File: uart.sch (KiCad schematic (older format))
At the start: 17 parts, among them P1 USB_OTG, U2 FOD817, U3 FOD817, U4 FOD817, U5 FOD817, U6 MCP2200, X1 CRYSTAL_SMD

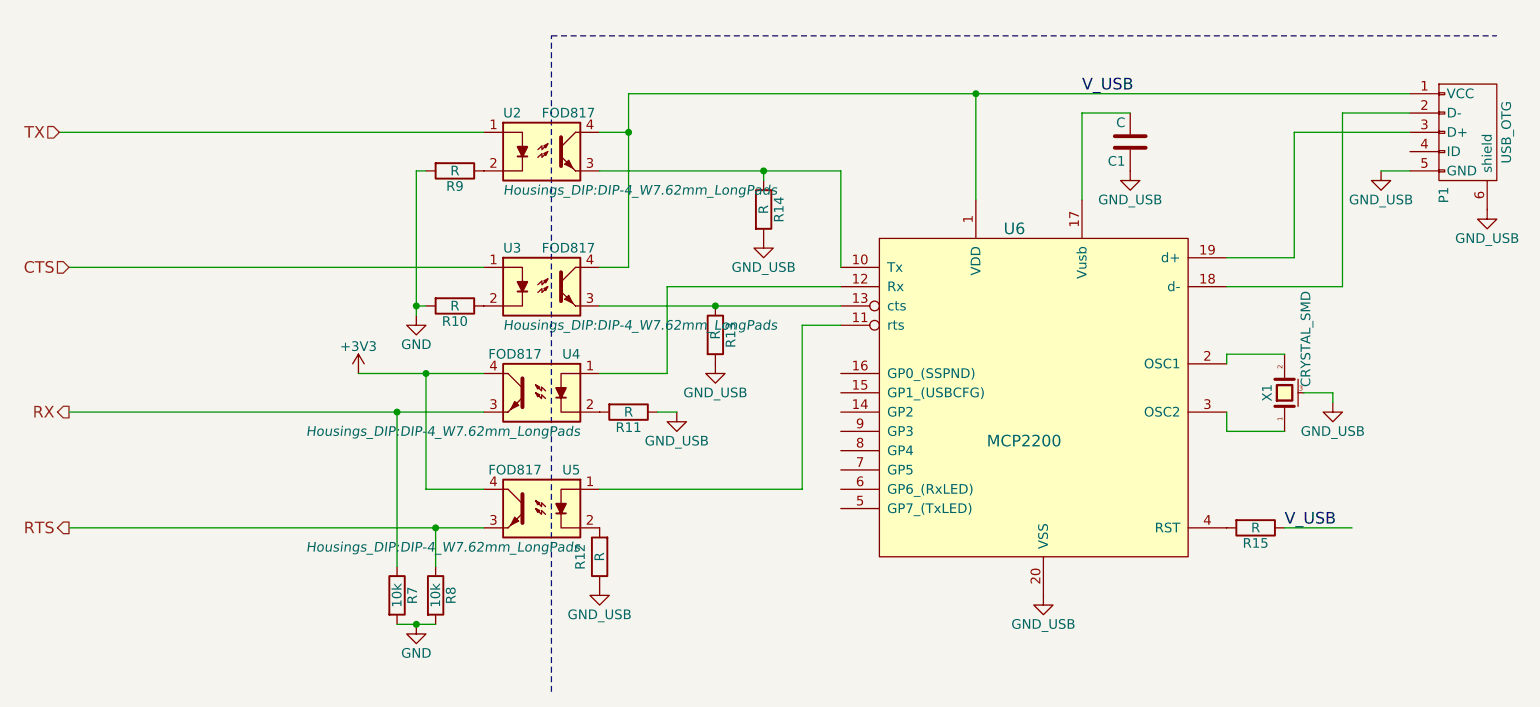
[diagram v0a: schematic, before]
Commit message: added 3 more h-bridges, and routed a bit
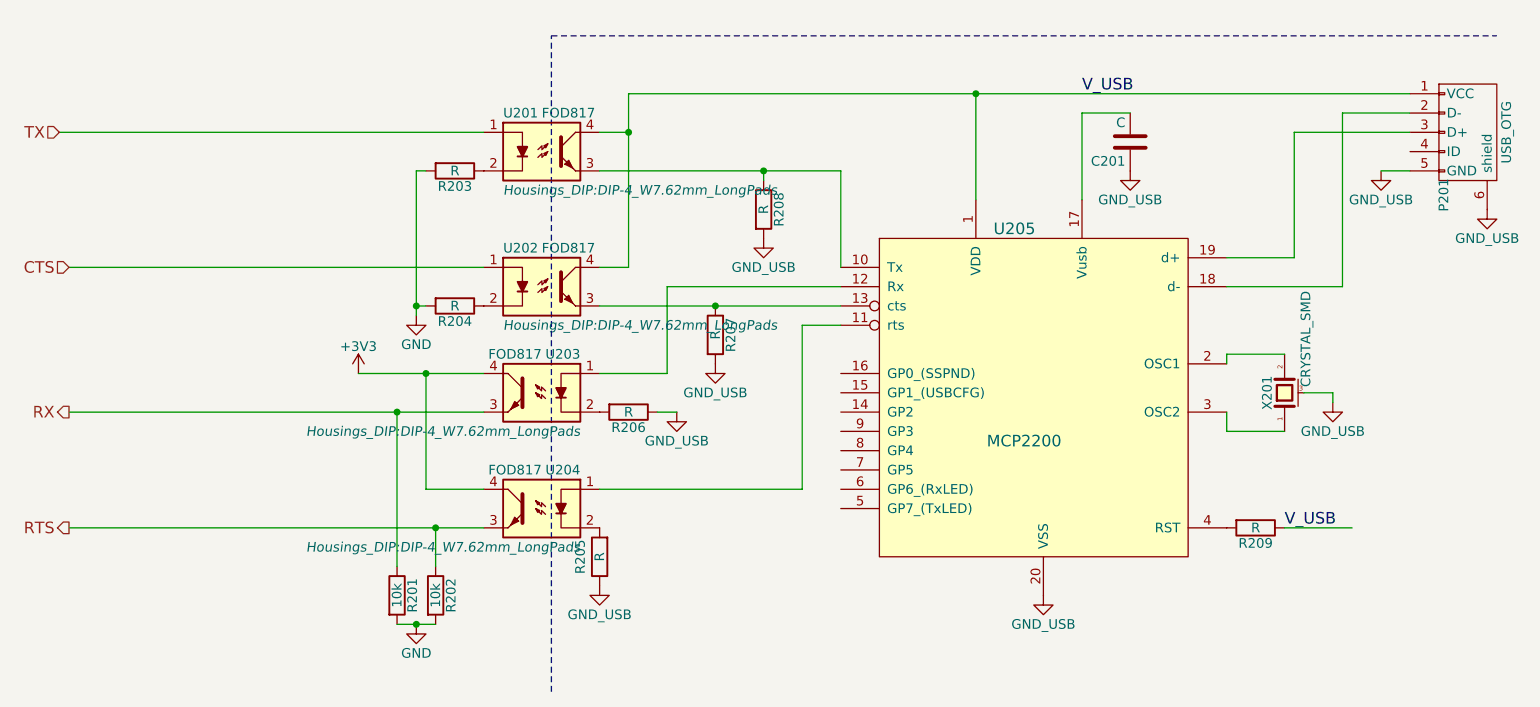
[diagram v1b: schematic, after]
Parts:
- renumbered C1 to C201, P1 to P201, R7 to R201, R8 to R202, R9 to R203, R10 to R204, R12 to R205, R11 to R206, R13 to R207, R14 to R208, R15 to R209, U2 to U201, U3 to U202, U4 to U203, U5 to U204, U6 to U205, X1 to X201
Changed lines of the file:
@@
 $Descr A4 11693 8268
 encoding utf-8
-Sheet 2 3
+Sheet 2 6
 Title ""
 Date ""
@@
 $EndDescr
 $Comp
-L CRYSTAL_SMD X1
+L CRYSTAL_SMD X201
 U 1 1 57226DD6
 P 9450 4650
-F 0 "X1" H 9450 4740 50  0000 C CNN
+F 0 "X201" H 9450 4740 50  0000 C CNN
 F 1 "CRYSTAL_SMD" H 9480 4540 50  0000 L CNN
 F 2 "TO_SOT_Packages_SMD:SOT89-3_Housing_Handsoldering" H 9450 4650 50  0001 C CNN
@@
 $EndComp
 $Comp
-L R R15
+L R R209
 U 1 1 57226DEA
 P 9300 5350
-F 0 "R15" V 9380 5350 50  0000 C CNN
+F 0 "R209" V 9380 5350 50  0000 C CNN
 F 1 "R" V 9300 5350 50  0000 C CNN
 F 2 "Resistors_SMD:R_0805_HandSoldering" V 9230 5350 50  0001 C CNN
@@
 V_USB
 $Comp
-L C C1
+L C C201
 U 1 1 57226DF4
 P 8650 3350
-F 0 "C1" H 8675 3450 50  0000 L CNN
+F 0 "C201" H 8675 3450 50  0000 L CNN
 F 1 "C" H 8675 3250 50  0000 L CNN
 F 2 "Capacitors_SMD:C_0805_HandSoldering" H 8688 3200 50  0001 C CNN
@@
 $EndComp
 $Comp
-L FOD817 U2
+L FOD817 U201
 U 1 1 57226DFC
 P 5600 3400
-F 0 "U2" H 5400 3600 50  0000 L CNN
+F 0 "U201" H 5400 3600 50  0000 L CNN
 F 1 "FOD817" H 5600 3600 50  0000 L CNN
 F 2 "Housings_DIP:DIP-4_W7.62mm_LongPads" H 5400 3200 50  0000 L CIN
@@
 $EndComp
 $Comp
-L FOD817 U3
+L FOD817 U202
 U 1 1 57226E03
 P 5600 4100
-F 0 "U3" H 5400 4300 50  0000 L CNN
+F 0 "U202" H 5400 4300 50  0000 L CNN
 F 1 "FOD817" H 5600 4300 50  0000 L CNN
 F 2 "Housings_DIP:DIP-4_W7.62mm_LongPads" H 5400 3900 50  0000 L CIN
@@
 $EndComp
 $Comp
-L FOD817 U4
+L FOD817 U203
 U 1 1 57226E0A
 P 5600 4650
-F 0 "U4" H 5400 4850 50  0000 L CNN
+F 0 "U203" H 5400 4850 50  0000 L CNN
 F 1 "FOD817" H 5600 4850 50  0000 L CNN
 F 2 "Housings_DIP:DIP-4_W7.62mm_LongPads" H 5400 4450 50  0000 L CIN
@@
 $EndComp
 $Comp
-L FOD817 U5
+L FOD817 U204
 U 1 1 57226E11
 P 5600 5250
-F 0 "U5" H 5400 5450 50  0000 L CNN
+F 0 "U204" H 5400 5450 50  0000 L CNN
 F 1 "FOD817" H 5600 5450 50  0000 L CNN
 F 2 "Housings_DIP:DIP-4_W7.62mm_LongPads" H 5400 5050 50  0000 L CIN
@@
 $EndComp
 $Comp
-L R R14
+L R R208
 U 1 1 57226E18
 P 6750 3700
-F 0 "R14" V 6830 3700 50  0000 C CNN
+F 0 "R208" V 6830 3700 50  0000 C CNN
 F 1 "R" V 6750 3700 50  0000 C CNN
 F 2 "Resistors_SMD:R_0805_HandSoldering" V 6680 3700 50  0001 C CNN
@@
 $EndComp
 $Comp
-L R R13
+L R R207
 U 1 1 57226E1F
 P 6500 4350
-F 0 "R13" V 6580 4350 50  0000 C CNN
+F 0 "R207" V 6580 4350 50  0000 C CNN
 F 1 "R" V 6500 4350 50  0000 C CNN
 F 2 "Resistors_SMD:R_0805_HandSoldering" V 6430 4350 50  0001 C CNN
@@
 $EndComp
 $Comp
-L R R11
+L R R206
 U 1 1 57226E26
 P 6050 4750
-F 0 "R11" V 6130 4750 50  0000 C CNN
+F 0 "R206" V 6130 4750 50  0000 C CNN
 F 1 "R" V 6050 4750 50  0000 C CNN
 F 2 "Resistors_SMD:R_0805_HandSoldering" V 5980 4750 50  0001 C CNN
@@
 	5900 4200 7150 4200
 $Comp
-L R R12
+L R R205
 U 1 1 57226E51
 P 5900 5500
-F 0 "R12" V 6000 5500 50  0000 C CNN
+F 0 "R205" V 6000 5500 50  0000 C CNN
 F 1 "R" V 5900 5500 50  0000 C CNN
 F 2 "Resistors_SMD:R_0805_HandSoldering" V 5830 5500 50  0001 C CNN
@@
 	5650 2800 10550 2800
 $Comp
-L R R8
+L R R202
 U 1 1 57226E69
 P 5050 5700
-F 0 "R8" V 5130 5700 50  0000 C CNN
+F 0 "R202" V 5130 5700 50  0000 C CNN
 F 1 "10k" V 5050 5700 50  0000 C CNN
 F 2 "Resistors_SMD:R_0805_HandSoldering" V 4980 5700 50  0001 C CNN
@@
 $EndComp
 $Comp
-L R R7
+L R R201
 U 1 1 57226E70
 P 4850 5700
-F 0 "R7" V 4930 5700 50  0000 C CNN
+F 0 "R201" V 4930 5700 50  0000 C CNN
 F 1 "10k" V 4850 5700 50  0000 C CNN
 F 2 "Resistors_SMD:R_0805_HandSoldering" V 4780 5700 50  0001 C CNN
@@
 Connection ~ 5000 4550
 $Comp
-L R R10
+L R R204
 U 1 1 57226E85
 P 5150 4200
-F 0 "R10" V 5230 4200 50  0000 C CNN
+F 0 "R204" V 5230 4200 50  0000 C CNN
 F 1 "R" V 5150 4200 50  0000 C CNN
 F 2 "Resistors_SMD:R_0805_HandSoldering" V 5080 4200 50  0001 C CNN
@@
 $EndComp
 $Comp
-L R R9
+L R R203
 U 1 1 57226E8C
 P 5150 3500
-F 0 "R9" V 5230 3500 50  0000 C CNN
+F 0 "R203" V 5230 3500 50  0000 C CNN
 F 1 "R" V 5150 3500 50  0000 C CNN
 F 2 "Resistors_SMD:R_0805_HandSoldering" V 5080 3500 50  0001 C CNN
@@
 	3150 4000 5300 4000
 $Comp
-L USB_OTG P1
+L USB_OTG P201
 U 1 1 5743537B
 P 10400 3300
-F 0 "P1" H 10725 3175 50  0000 C CNN
+F 0 "P201" H 10725 3175 50  0000 C CNN
 F 1 "USB_OTG" H 10400 3500 50  0000 C CNN
 F 2 "Connect:USB_Micro-B" V 10350 3200 50  0001 C CNN
@@
 $EndComp
 $Comp
-L MCP2200 U6
+L MCP2200 U205
 U 1 1 57226DCF
 P 8200 5500
-F 0 "U6" H 8050 7200 60  0000 C CNN
+F 0 "U205" H 8050 7200 60  0000 C CNN
 F 1 "MCP2200" H 8100 6100 60  0000 C CNN
 F 2 "Housings_SOIC:SOIC-20_7.5x12.8mm_Pitch1.27mm" H 8200 5500 60  0001 C CNN

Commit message: Added requirements
Also selected components for certain things.
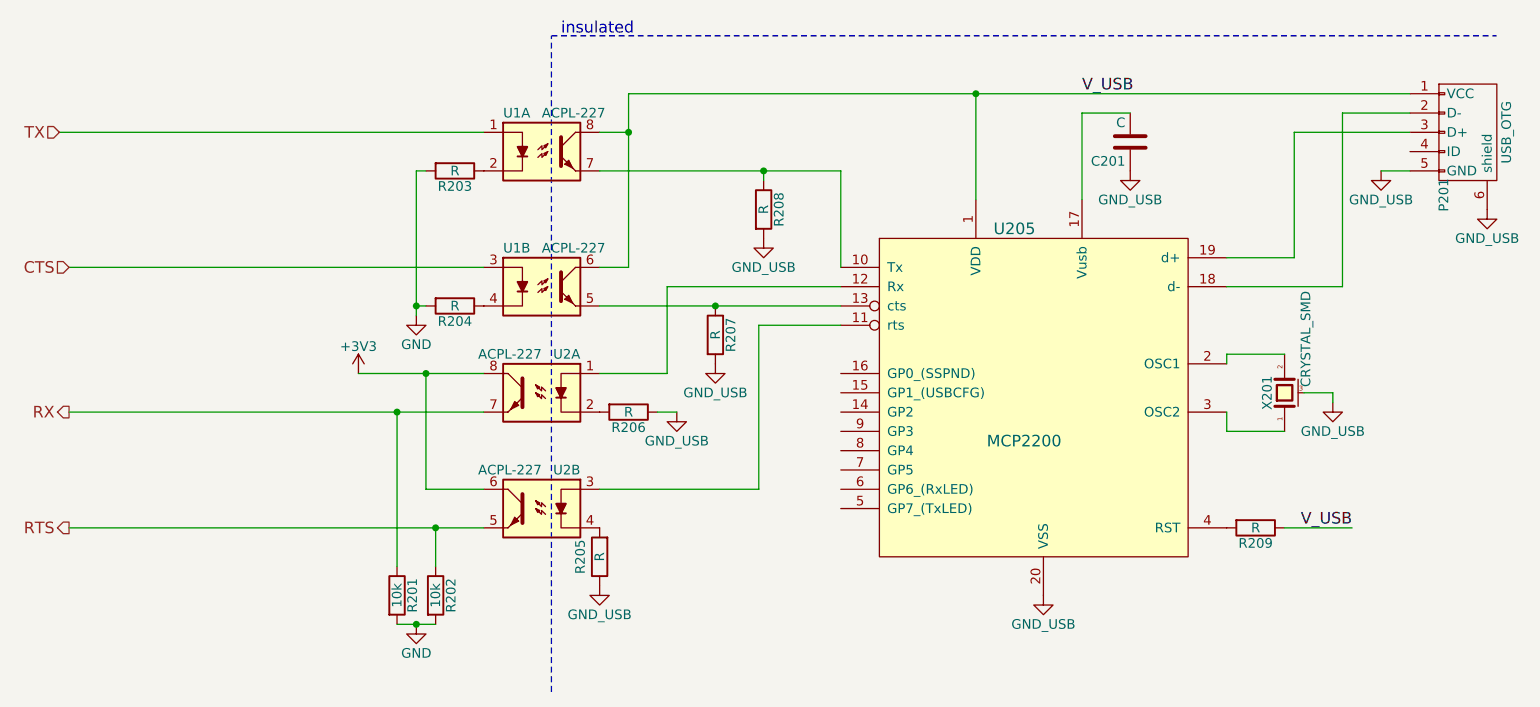
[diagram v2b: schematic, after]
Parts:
- removed U201, U202, U203, U204: FOD817, Housings_DIP:DIP-4_W7.62mm_LongPads, symbol FOD817
- added U1, U2: ACPL-227, SMD_Packages:SOIC-8-N, symbol ACPL-227
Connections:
- net +3V3: now also U2.6, U2.8
- net CTS: now also U1.3
- net RTS: now also U2.5
- net RX: now also U2.7
- net TX: now also U1.1
- net V_USB: now also U1.6, U1.8
- net at R208.1, U205.10 (Tx): now also U1.7
- net at U205.11 (rts): now also U2.3
- net at U205.12 (Rx): now also U2.1
- net at R207.1, U205.13 (cts): now also U1.5
- net at R203.1: now also U1.2
- net at R204.1: now also U1.4
- net at R206.2: now also U2.2
- net at R205.2: now also U2.4
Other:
- note added: "insulated"
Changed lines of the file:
@@
 $Descr A4 11693 8268
 encoding utf-8
-Sheet 2 6
+Sheet 2 7
 Title ""
 Date ""
@@
 Text Label 8400 3100 0    60   ~ 0
 V_USB
-Text Label 9450 5350 0    60   ~ 0
+Text Label 9800 5350 2    60   ~ 0
 V_USB
 $Comp
@@
 $EndComp
 $Comp
-L FOD817 U201
-U 1 1 57226DFC
-P 5600 3400
-F 0 "U201" H 5400 3600 50  0000 L CNN
-F 1 "FOD817" H 5600 3600 50  0000 L CNN
-F 2 "Housings_DIP:DIP-4_W7.62mm_LongPads" H 5400 3200 50  0000 L CIN
-F 3 "" H 5600 3400 50  0000 L CNN
-	1    5600 3400
-	1    0    0    -1
-$EndComp
-$Comp
-L FOD817 U202
-U 1 1 57226E03
-P 5600 4100
-F 0 "U202" H 5400 4300 50  0000 L CNN
-F 1 "FOD817" H 5600 4300 50  0000 L CNN
-F 2 "Housings_DIP:DIP-4_W7.62mm_LongPads" H 5400 3900 50  0000 L CIN
-F 3 "" H 5600 4100 50  0000 L CNN
-	1    5600 4100
-	1    0    0    -1
-$EndComp
-$Comp
-L FOD817 U203
-U 1 1 57226E0A
-P 5600 4650
-F 0 "U203" H 5400 4850 50  0000 L CNN
-F 1 "FOD817" H 5600 4850 50  0000 L CNN
-F 2 "Housings_DIP:DIP-4_W7.62mm_LongPads" H 5400 4450 50  0000 L CIN
-F 3 "" H 5600 4650 50  0000 L CNN
-	1    5600 4650
-	-1   0    0    -1
-$EndComp
-$Comp
-L FOD817 U204
-U 1 1 57226E11
-P 5600 5250
-F 0 "U204" H 5400 5450 50  0000 L CNN
-F 1 "FOD817" H 5600 5450 50  0000 L CNN
-F 2 "Housings_DIP:DIP-4_W7.62mm_LongPads" H 5400 5050 50  0000 L CIN
-F 3 "" H 5600 5250 50  0000 L CNN
-	1    5600 5250
-	-1   0    0    -1
-$EndComp
-$Comp
 L R R208
 U 1 1 57226E18
@@
 Connection ~ 6500 4200
 Wire Wire Line
-	7150 4300 6950 4300
-Wire Wire Line
-	6950 4300 6950 5150
-Wire Wire Line
-	6950 5150 5900 5150
+	7150 4300 6725 4300
+Wire Wire Line
+	6725 4300 6725 5150
+Wire Wire Line
+	6725 5150 5900 5150
 Wire Notes Line
 	5650 6200 5650 2800
@@
 	1    0    0    -1
 $EndComp
+$Comp
+L ACPL-227 U1
+U 1 1 57BD68E3
+P 5600 3400
+F 0 "U1" H 5400 3600 50  0000 L CNN
+F 1 "ACPL-227" H 5600 3600 50  0000 L CNN
+F 2 "SMD_Packages:SOIC-8-N" H 5400 3200 50  0001 L CIN
+F 3 "" H 5400 3600 50  0000 L CNN
+	1    5600 3400
+	1    0    0    -1
+$EndComp
+$Comp
+L ACPL-227 U1
+U 2 1 57BD69FE
+P 5600 4100
+F 0 "U1" H 5400 4300 50  0000 L CNN
+F 1 "ACPL-227" H 5600 4300 50  0000 L CNN
+F 2 "SMD_Packages:SOIC-8-N" H 5400 3900 50  0001 L CIN
+F 3 "" H 5400 4300 50  0000 L CNN
+	2    5600 4100
+	1    0    0    -1
+$EndComp
+$Comp
+L ACPL-227 U2
+U 1 1 57BD6ABC
+P 5600 4650
+F 0 "U2" H 5400 4850 50  0000 L CNN
+F 1 "ACPL-227" H 5600 4850 50  0000 L CNN
+F 2 "SMD_Packages:SOIC-8-N" H 5400 4450 50  0001 L CIN
+F 3 "" H 5400 4850 50  0000 L CNN
+	1    5600 4650
+	-1   0    0    -1
+$EndComp
+$Comp
+L ACPL-227 U2
+U 2 1 57BD6C05
+P 5600 5250
+F 0 "U2" H 5400 5450 50  0000 L CNN
+F 1 "ACPL-227" H 5600 5450 50  0000 L CNN
+F 2 "SMD_Packages:SOIC-8-N" H 5400 5050 50  0001 L CIN
+F 3 "" H 5400 5450 50  0000 L CNN
+	2    5600 5250
+	-1   0    0    -1
+$EndComp
+Text Notes 5700 2800 0    60   ~ 0
+insulated
 $EndSCHEMATC

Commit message: Routed a h-bridge. Damn that's a lot of work.
also assigned a lot of components.
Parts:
- R201, R202, R203, R204, R205, R206, R207, R208, R209: footprint Resistors_SMD:R_0805_HandSoldering -> lib:R_0402_handsoldering
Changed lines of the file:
@@
 $Descr A4 11693 8268
 encoding utf-8
-Sheet 2 7
+Sheet 2 8
 Title ""
 Date ""
@@
 F 0 "R209" V 9380 5350 50  0000 C CNN
 F 1 "R" V 9300 5350 50  0000 C CNN
-F 2 "Resistors_SMD:R_0805_HandSoldering" V 9230 5350 50  0001 C CNN
+F 2 "lib:R_0402_handsoldering" V 9230 5350 50  0001 C CNN
 F 3 "" H 9300 5350 50  0000 C CNN
 	1    9300 5350
@@
 F 0 "R208" V 6830 3700 50  0000 C CNN
 F 1 "R" V 6750 3700 50  0000 C CNN
-F 2 "Resistors_SMD:R_0805_HandSoldering" V 6680 3700 50  0001 C CNN
+F 2 "lib:R_0402_handsoldering" V 6680 3700 50  0001 C CNN
 F 3 "" H 6750 3700 50  0000 C CNN
 	1    6750 3700
@@
 F 0 "R207" V 6580 4350 50  0000 C CNN
 F 1 "R" V 6500 4350 50  0000 C CNN
-F 2 "Resistors_SMD:R_0805_HandSoldering" V 6430 4350 50  0001 C CNN
+F 2 "lib:R_0402_handsoldering" V 6430 4350 50  0001 C CNN
 F 3 "" H 6500 4350 50  0000 C CNN
 	1    6500 4350
@@
 F 0 "R206" V 6130 4750 50  0000 C CNN
 F 1 "R" V 6050 4750 50  0000 C CNN
-F 2 "Resistors_SMD:R_0805_HandSoldering" V 5980 4750 50  0001 C CNN
+F 2 "lib:R_0402_handsoldering" V 5980 4750 50  0001 C CNN
 F 3 "" H 6050 4750 50  0000 C CNN
 	1    6050 4750
@@
 F 0 "R205" V 6000 5500 50  0000 C CNN
 F 1 "R" V 5900 5500 50  0000 C CNN
-F 2 "Resistors_SMD:R_0805_HandSoldering" V 5830 5500 50  0001 C CNN
+F 2 "lib:R_0402_handsoldering" V 5830 5500 50  0001 C CNN
 F 3 "" H 5900 5500 50  0000 C CNN
 	1    5900 5500
@@
 F 0 "R202" V 5130 5700 50  0000 C CNN
 F 1 "10k" V 5050 5700 50  0000 C CNN
-F 2 "Resistors_SMD:R_0805_HandSoldering" V 4980 5700 50  0001 C CNN
+F 2 "lib:R_0402_handsoldering" V 4980 5700 50  0001 C CNN
 F 3 "" H 5050 5700 50  0000 C CNN
 	1    5050 5700
@@
 F 0 "R201" V 4930 5700 50  0000 C CNN
 F 1 "10k" V 4850 5700 50  0000 C CNN
-F 2 "Resistors_SMD:R_0805_HandSoldering" V 4780 5700 50  0001 C CNN
+F 2 "lib:R_0402_handsoldering" V 4780 5700 50  0001 C CNN
 F 3 "" H 4850 5700 50  0000 C CNN
 	1    4850 5700
@@
 	3150 4750 5300 4750
 $Comp
-L +3V3 #PWR09
+L +3V3 #PWR011
 U 1 1 57226E7B
 P 4650 4550
-F 0 "#PWR09" H 4650 4400 50  0001 C CNN
+F 0 "#PWR011" H 4650 4400 50  0001 C CNN
 F 1 "+3V3" H 4650 4690 50  0000 C CNN
 F 2 "" H 4650 4550 50  0000 C CNN
@@
 F 0 "R204" V 5230 4200 50  0000 C CNN
 F 1 "R" V 5150 4200 50  0000 C CNN
-F 2 "Resistors_SMD:R_0805_HandSoldering" V 5080 4200 50  0001 C CNN
+F 2 "lib:R_0402_handsoldering" V 5080 4200 50  0001 C CNN
 F 3 "" H 5150 4200 50  0000 C CNN
 	1    5150 4200
@@
 F 0 "R203" V 5230 3500 50  0000 C CNN
 F 1 "R" V 5150 3500 50  0000 C CNN
-F 2 "Resistors_SMD:R_0805_HandSoldering" V 5080 3500 50  0001 C CNN
+F 2 "lib:R_0402_handsoldering" V 5080 3500 50  0001 C CNN
 F 3 "" H 5150 3500 50  0000 C CNN
 	1    5150 3500
@@
 $EndComp
 $Comp
-L GND #PWR010
+L GND #PWR012
 U 1 1 57226E93
 P 4950 5850
-F 0 "#PWR010" H 4950 5600 50  0001 C CNN
+F 0 "#PWR012" H 4950 5600 50  0001 C CNN
 F 1 "GND" H 4950 5700 50  0000 C CNN
 F 2 "" H 4950 5850 50  0000 C CNN
@@
 Connection ~ 4950 5850
 $Comp
-L GND #PWR011
+L GND #PWR013
 U 1 1 57226E9B
 P 4950 4250
-F 0 "#PWR011" H 4950 4000 50  0001 C CNN
+F 0 "#PWR013" H 4950 4000 50  0001 C CNN
 F 1 "GND" H 4950 4100 50  0000 C CNN
 F 2 "" H 4950 4250 50  0000 C CNN
@@
 	9950 3500 10100 3500
 $Comp
-L GND_USB #PWR012
+L GND_USB #PWR014
 U 1 1 575EC395
 P 5900 5650
-F 0 "#PWR012" H 5900 5400 50  0001 C CNN
+F 0 "#PWR014" H 5900 5400 50  0001 C CNN
 F 1 "GND_USB" H 5900 5500 50  0000 C CNN
 F 2 "" H 5900 5650 50  0000 C CNN
@@
 $EndComp
 $Comp
-L GND_USB #PWR013
+L GND_USB #PWR015
 U 1 1 575EC6F9
 P 8200 5700
-F 0 "#PWR013" H 8200 5450 50  0001 C CNN
+F 0 "#PWR015" H 8200 5450 50  0001 C CNN
 F 1 "GND_USB" H 8200 5550 50  0000 C CNN
 F 2 "" H 8200 5700 50  0000 C CNN
@@
 $EndComp
 $Comp
-L GND_USB #PWR014
+L GND_USB #PWR016
 U 1 1 575EC8E8
 P 9950 3500
-F 0 "#PWR014" H 9950 3250 50  0001 C CNN
+F 0 "#PWR016" H 9950 3250 50  0001 C CNN
 F 1 "GND_USB" H 9950 3350 50  0000 C CNN
 F 2 "" H 9950 3500 50  0000 C CNN
@@
 $EndComp
 $Comp
-L GND_USB #PWR015
+L GND_USB #PWR017
 U 1 1 575EC980
 P 8650 3500
-F 0 "#PWR015" H 8650 3250 50  0001 C CNN
+F 0 "#PWR017" H 8650 3250 50  0001 C CNN
 F 1 "GND_USB" H 8650 3350 50  0000 C CNN
 F 2 "" H 8650 3500 50  0000 C CNN
@@
 	8400 3200 8650 3200
 $Comp
-L GND_USB #PWR016
+L GND_USB #PWR018
 U 1 1 575ECD4E
 P 6300 4750
-F 0 "#PWR016" H 6300 4500 50  0001 C CNN
+F 0 "#PWR018" H 6300 4500 50  0001 C CNN
 F 1 "GND_USB" H 6300 4600 50  0000 C CNN
 F 2 "" H 6300 4750 50  0000 C CNN
@@
 	6300 4750 6200 4750
 $Comp
-L GND_USB #PWR017
+L GND_USB #PWR019
 U 1 1 575ED02E
 P 6500 4500
-F 0 "#PWR017" H 6500 4250 50  0001 C CNN
+F 0 "#PWR019" H 6500 4250 50  0001 C CNN
 F 1 "GND_USB" H 6500 4350 50  0000 C CNN
 F 2 "" H 6500 4500 50  0000 C CNN
@@
 $EndComp
 $Comp
-L GND_USB #PWR018
+L GND_USB #PWR020
 U 1 1 575ED06C
 P 6750 3850
-F 0 "#PWR018" H 6750 3600 50  0001 C CNN
+F 0 "#PWR020" H 6750 3600 50  0001 C CNN
 F 1 "GND_USB" H 6750 3700 50  0000 C CNN
 F 2 "" H 6750 3850 50  0000 C CNN
@@
 	4950 3500 5000 3500
 $Comp
-L GND_USB #PWR019
+L GND_USB #PWR021
 U 1 1 575EDAA2
 P 10500 3700
-F 0 "#PWR019" H 10500 3450 50  0001 C CNN
+F 0 "#PWR021" H 10500 3450 50  0001 C CNN
 F 1 "GND_USB" H 10500 3550 50  0000 C CNN
 F 2 "" H 10500 3700 50  0000 C CNN
@@
 $EndComp
 $Comp
-L GND_USB #PWR020
+L GND_USB #PWR022
 U 1 1 575F0AA5
 P 9700 4700
-F 0 "#PWR020" H 9700 4450 50  0001 C CNN
+F 0 "#PWR022" H 9700 4450 50  0001 C CNN
 F 1 "GND_USB" H 9700 4550 50  0000 C CNN
 F 2 "" H 9700 4700 50  0000 C CNN
